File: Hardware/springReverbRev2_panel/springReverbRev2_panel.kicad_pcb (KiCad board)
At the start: 2 copper layers, 100 x 200 mm, 21 parts

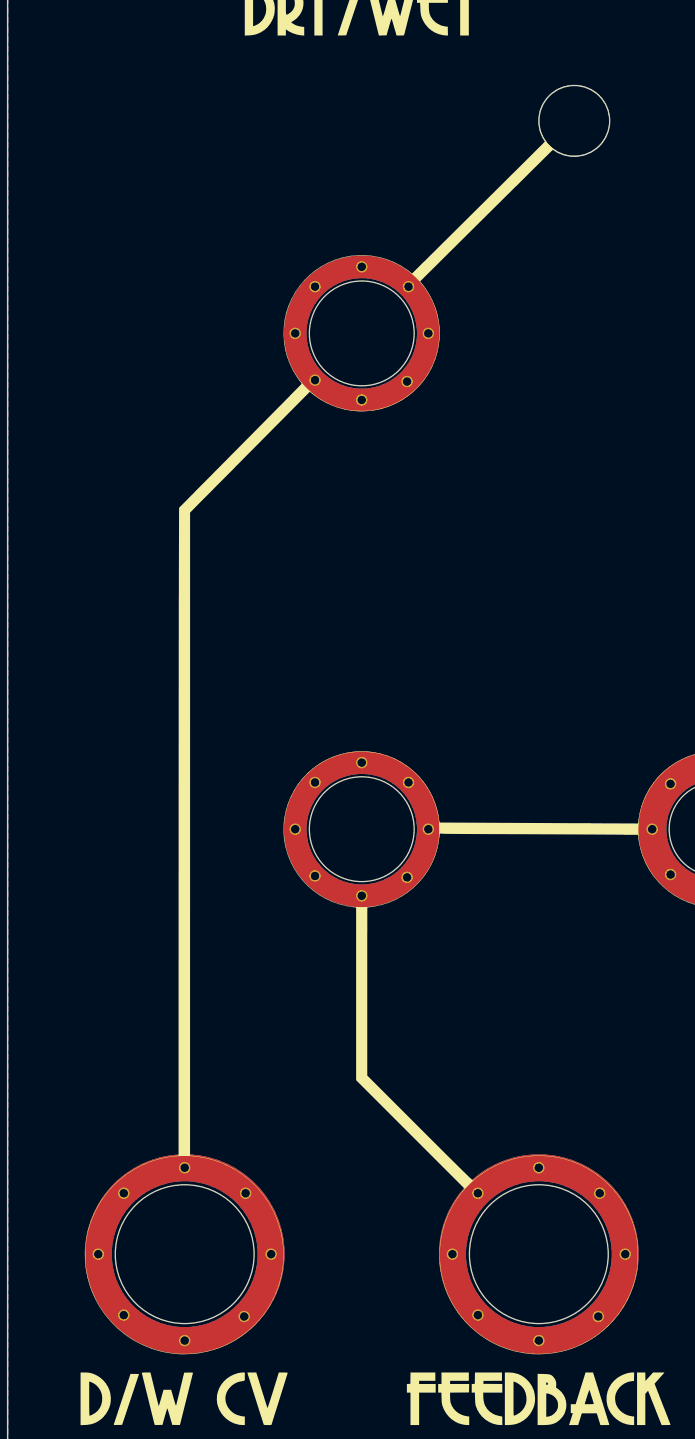
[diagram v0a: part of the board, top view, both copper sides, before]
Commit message: Docs; make LED position consistent
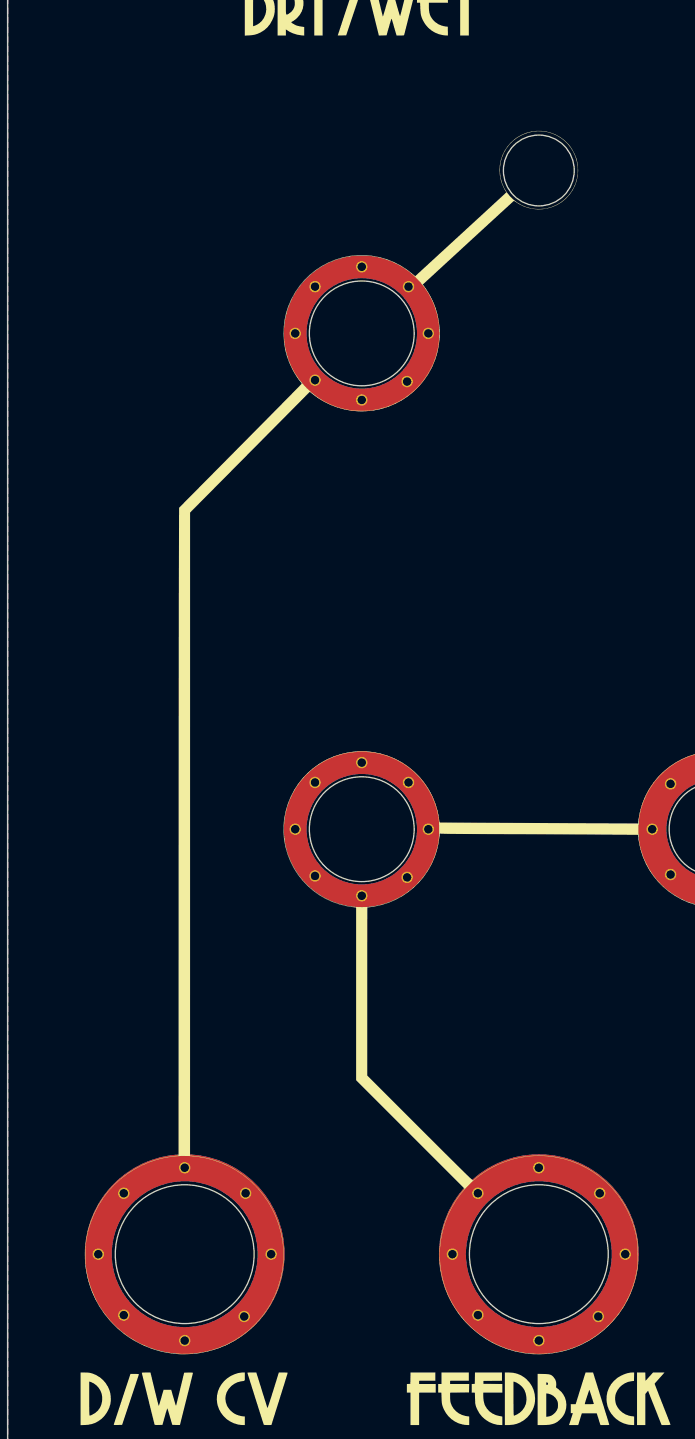
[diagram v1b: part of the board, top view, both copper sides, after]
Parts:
- moved H13 4.30 mm to (103.6, 131.1)

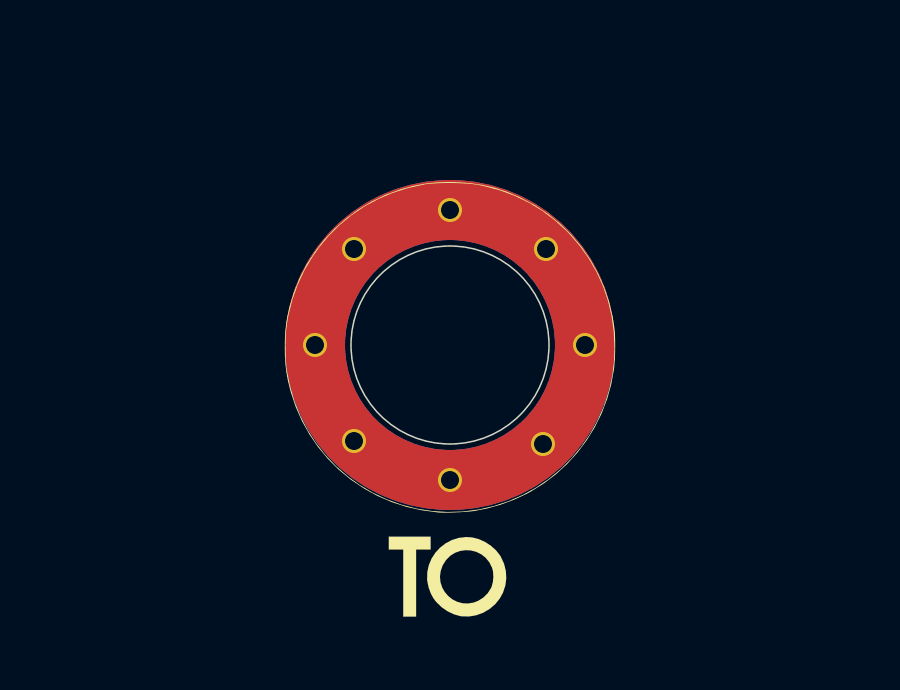
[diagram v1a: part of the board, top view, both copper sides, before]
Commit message: Ungrounded jack for tank send
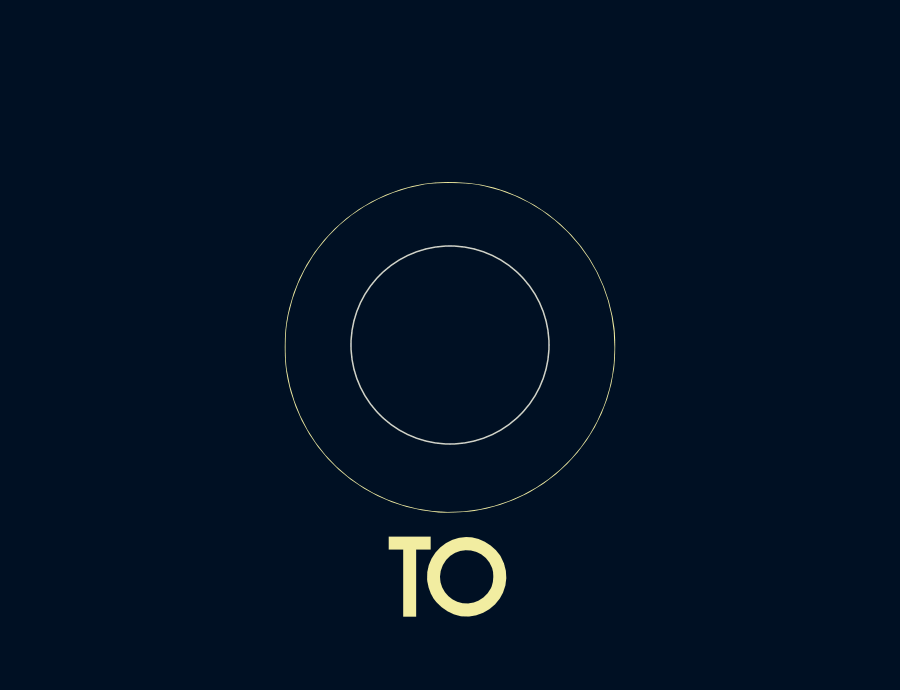
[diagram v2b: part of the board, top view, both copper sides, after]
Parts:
- H18: value RCA_Jack_Hole -> Nongrounded_Jack_Hole; footprint springReverbRev2_panel:Kosmo_RCA_Jack_Hole -> springReverbRev2_panel:Kosmo_Nongrounded_RCA_Jack_Hole
- moved H17 25.0 mm to (128.6, 232.6)
- moved H18 25.0 mm to (103.6, 232.6)
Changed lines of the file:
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@@
       (net 1 "GND") (pintype "passive") (zone_connect 2))
   )
-  (footprint "springReverbRev2_panel:Kosmo_RCA_Jack_Hole" (layer "F.Cu")
-    (at 128.6 232.6)
+  (footprint "springReverbRev2_panel:Kosmo_Nongrounded_RCA_Jack_Hole" (layer "F.Cu")
+    (at 103.6 232.6)
     (descr "Dailywell M1 series")
     (tags "Dailywell M1 series")
     (property "Sheetfile" "springReverbRev2_panel.kicad_sch")
     (property "Sheetname" "")
-    (property "exclude_from_bom" "")
-    (attr exclude_from_pos_files exclude_from_bom)
+    (attr exclude_from_pos_files)
     (fp_text reference "H18" (at 0 -7) (layer "F.SilkS") hide
         (effects (font (size 1 1) (thickness 0.15)))
     )
-    (fp_text value "RCA_Jack_Hole" (at 0 8.3) (layer "F.Fab")
+    (fp_text value "Nongrounded_Jack_Hole" (at 0 8.3) (layer "F.Fab")
         (effects (font (size 1 1) (thickness 0.15)))
     )
@@
     (fp_circle (center 0 0) (end 7.2 0)
       (stroke (width 0.05) (type solid)) (fill none) (layer "F.CrtYd"))
-    (pad "1" smd custom (at -4.5 0) (size 0.5 0.5) (layers "F.Cu" "F.Paste" "F.Mask")
-      (net 1 "GND") (pintype "passive") (zone_connect 2) (thermal_bridge_angle 45)
-      (options (clearance outline) (anchor circle))
-      (primitives
-        (gr_circle (center 4.5 0) (end 9 0) (width 2) (fill none))
-      ))
-    (pad "1" smd custom (at -4.5 0) (size 0.5 0.5) (layers "B.Cu" "B.Paste" "B.Mask")
-      (net 1 "GND") (pintype "passive") (zone_connect 2) (thermal_bridge_angle 45)
-      (options (clearance outline) (anchor circle))
-      (primitives
-        (gr_circle (center 4.5 0) (end 9 0) (width 2) (fill none))
-      ))
-    (pad "1" thru_hole circle (at -4.5 0) (size 0.8 0.8) (drill 0.6) (layers "*.Mask" "F.Cu" "In1.Cu" "B.Cu")
-      (net 1 "GND") (pintype "passive"))
-    (pad "1" thru_hole circle (at -3.2 -3.2) (size 0.8 0.8) (drill 0.6) (layers "*.Mask" "F.Cu" "In1.Cu" "B.Cu")
-      (net 1 "GND") (pintype "passive"))
-    (pad "1" thru_hole circle (at -3.2 3.2) (size 0.8 0.8) (drill 0.6) (layers "*.Mask" "F.Cu" "In1.Cu" "B.Cu")
-      (net 1 "GND") (pintype "passive"))
-    (pad "1" thru_hole circle (at 0 -4.5) (size 0.8 0.8) (drill 0.6) (layers "*.Mask" "F.Cu" "In1.Cu" "B.Cu")
-      (net 1 "GND") (pintype "passive"))
-    (pad "1" thru_hole circle (at 0 4.5) (size 0.8 0.8) (drill 0.6) (layers "*.Mask" "F.Cu" "In1.Cu" "B.Cu")
-      (net 1 "GND") (pintype "passive"))
-    (pad "1" thru_hole circle (at 3.1 3.3) (size 0.8 0.8) (drill 0.6) (layers "*.Mask" "F.Cu" "In1.Cu" "B.Cu")
-      (net 1 "GND") (pintype "passive"))
-    (pad "1" thru_hole circle (at 3.2 -3.2) (size 0.8 0.8) (drill 0.6) (layers "*.Mask" "F.Cu" "In1.Cu" "B.Cu")
-      (net 1 "GND") (pintype "passive"))
-    (pad "1" thru_hole circle (at 4.5 0) (size 0.8 0.8) (drill 0.6) (layers "*.Mask" "F.Cu" "In1.Cu" "B.Cu")
-      (net 1 "GND") (pintype "passive"))
   )
   (footprint "Kosmo_panel:Kosmo_Pot_Hole" (layer "F.Cu")
@@
   )
   (footprint "springReverbRev2_panel:Kosmo_RCA_Jack_Hole" (layer "F.Cu")
-    (at 103.6 232.6)
+    (at 128.6 232.6)
     (descr "Dailywell M1 series")
     (tags "Dailywell M1 series")
